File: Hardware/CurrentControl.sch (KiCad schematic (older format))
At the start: 24 parts, among them J4 Screw_Terminal_01x02, Q1 PSMN5R2-60YL, U3 DAC121C081CIMK, U4 TLV9102IPWR

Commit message: forgot to save
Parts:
- removed C16: 1n, Capacitor_SMD:C_0603_1608Metric_Pad1.05x0.95mm_HandSolder, symbol Device:C_Small
- removed U4: TLV9102IPWR, Package_SO:TSSOP-8_4.4x3mm_P0.65mm, symbol E-Load-rescue:TLV9102IPWR
- added R24: 5.6k, Resistor_SMD:R_0603_1608Metric_Pad1.05x0.95mm_HandSolder, symbol Device:R_Small
- added R26: 50k, Resistor_SMD:R_0603_1608Metric_Pad1.05x0.95mm_HandSolder, symbol Device:R_Small
- added TP1: TestPoint_Alt, TestPoint:TestPoint_Keystone_5000-5004_Miniature, symbol Connector:TestPoint_Alt
- added U4: MCP6H04, Package_SO:TSSOP-14_4.4x5mm_P0.65mm, symbol E-Load-rescue:MCP6H04
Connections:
- net labels added: Current_ADC, Vin_ADC
- net labels removed: ADC
- wire segments 60 -> 93
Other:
- moved on the sheet: C13, C15, C17, Q1, R10, R11, R12, R13, R20, R23, R25, R4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

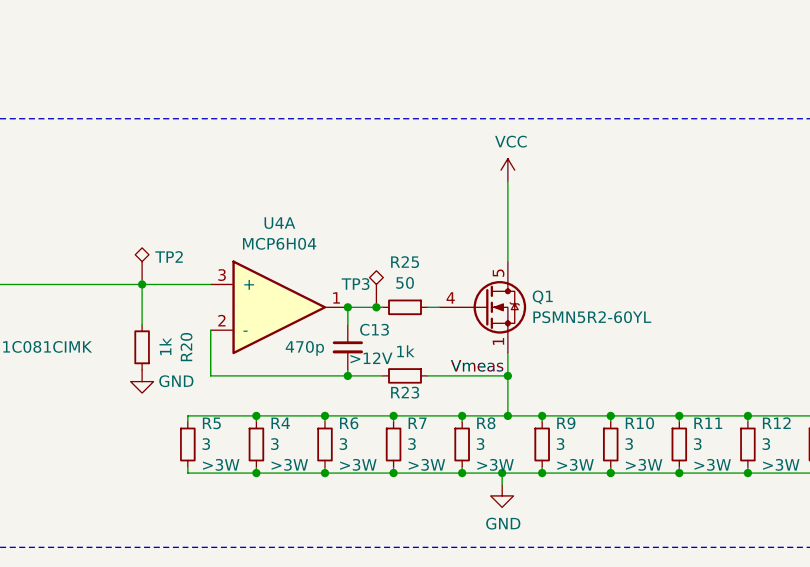
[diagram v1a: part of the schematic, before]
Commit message: Added LCSC part#, Thermal vias, etc
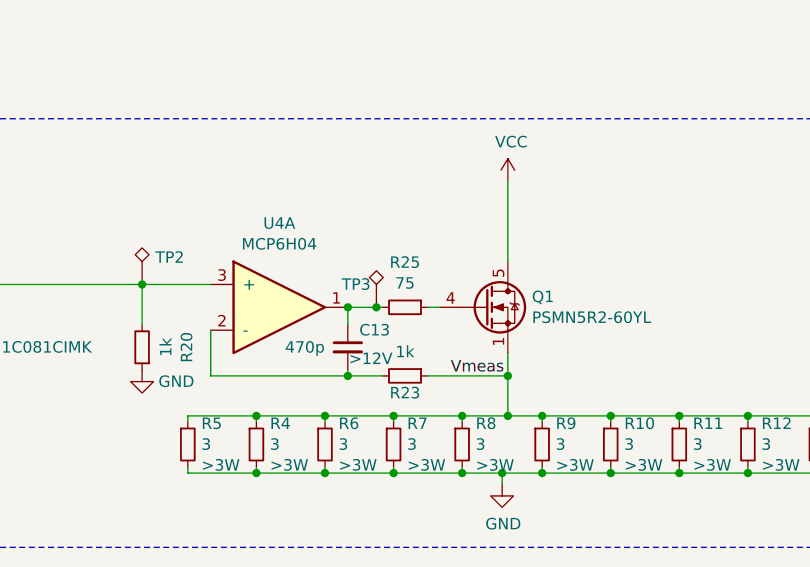
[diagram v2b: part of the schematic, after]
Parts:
- C13: LCSC (none) -> C376836
- C15, C17: LCSC (none) -> C100040
- J4: footprint Connector_TE-Connectivity:TE_826576-2_1x02_P3.96mm_Vertical -> Connector_Phoenix_MC:PhoenixContact_MCV_1,5_2-G-3.81_1x02_P3.81mm_Vertical; LCSC (none) -> C89123
- Q1: Digikey (none) -> 1727-2595-1-ND
- R10, R11, R12, R13, R4, R5, R6, R7, R8, R9: Digikey (none) -> PPC5W3.0CT-ND
- R20, R23: LCSC (none) -> C441891
- R24: LCSC (none) -> C507469
- R25: value 50 -> 75; LCSC (none) -> C441884
- R26: LCSC (none) -> C881419
- U3: Digikey (none) -> DAC121C081CIMK/NOPBCT-ND
- U4: Digikey (none) -> MCP6H04T-E/SLCT-ND
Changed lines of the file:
@@
 F 3 "~" H 3275 3850 50  0001 C CNN
 F 4 ">3W" H 3334 3759 50  0000 L CNN "Power "
+F 5 "PPC5W3.0CT-ND" H 3275 3850 50  0001 C CNN "Digikey"
 	1    3275 3850
 	1    0    0    -1
@@
 F 3 "~" H 3575 3850 50  0001 C CNN
 F 4 ">3W" H 3634 3759 50  0000 L CNN "Power "
+F 5 "PPC5W3.0CT-ND" H 3575 3850 50  0001 C CNN "Digikey"
 	1    3575 3850
 	1    0    0    -1
@@
 F 3 "~" H 3875 3850 50  0001 C CNN
 F 4 ">3W" H 3934 3759 50  0000 L CNN "Power "
+F 5 "PPC5W3.0CT-ND" H 3875 3850 50  0001 C CNN "Digikey"
 	1    3875 3850
 	1    0    0    -1
@@
 F 3 "~" H 4175 3850 50  0001 C CNN
 F 4 ">3W" H 4234 3759 50  0000 L CNN "Power "
+F 5 "PPC5W3.0CT-ND" H 4175 3850 50  0001 C CNN "Digikey"
 	1    4175 3850
 	1    0    0    -1
@@
 F 3 "~" H 4525 3850 50  0001 C CNN
 F 4 ">3W" H 4584 3759 50  0000 L CNN "Power "
+F 5 "PPC5W3.0CT-ND" H 4525 3850 50  0001 C CNN "Digikey"
 	1    4525 3850
 	1    0    0    -1
@@
 F 3 "~" H 4825 3850 50  0001 C CNN
 F 4 ">3W" H 4884 3759 50  0000 L CNN "Power "
+F 5 "PPC5W3.0CT-ND" H 4825 3850 50  0001 C CNN "Digikey"
 	1    4825 3850
 	1    0    0    -1
@@
 F 3 "~" H 5125 3850 50  0001 C CNN
 F 4 ">3W" H 5184 3759 50  0000 L CNN "Power "
+F 5 "PPC5W3.0CT-ND" H 5125 3850 50  0001 C CNN "Digikey"
 	1    5125 3850
 	1    0    0    -1
@@
 F 3 "~" H 5425 3850 50  0001 C CNN
 F 4 ">3W" H 5484 3759 50  0000 L CNN "Power "
+F 5 "PPC5W3.0CT-ND" H 5425 3850 50  0001 C CNN "Digikey"
 	1    5425 3850
 	1    0    0    -1
@@
 F 3 "~" H 5725 3850 50  0001 C CNN
 F 4 ">3W" H 5784 3759 50  0000 L CNN "Power "
+F 5 "PPC5W3.0CT-ND" H 5725 3850 50  0001 C CNN "Digikey"
 	1    5725 3850
 	1    0    0    -1
@@
 F 3 "~" H 2975 3850 50  0001 C CNN
 F 4 ">3W" H 3034 3759 50  0000 L CNN "Power "
+F 5 "PPC5W3.0CT-ND" H 2975 3850 50  0001 C CNN "Digikey"
 	1    2975 3850
 	1    0    0    -1
@@
 F 3 "~" H 10225 2950 50  0001 C CNN
 F 4 ">12V" H 10325 2850 50  0000 C CNN "Voltage"
+F 5 "" H 10225 2950 50  0001 C CNN "Digikey"
+F 6 "C100040" H 10225 2950 50  0001 C CNN "LCSC"
 	1    10225 2950
 	1    0    0    -1
@@
 P 3925 3250
 F 0 "R25" V 3729 3250 50  0000 C CNN
-F 1 "50" V 3820 3250 50  0000 C CNN
+F 1 "75" V 3820 3250 50  0000 C CNN
 F 2 "Resistor_SMD:R_0603_1608Metric_Pad1.05x0.95mm_HandSolder" H 3925 3250 50  0001 C CNN
 F 3 "~" H 3925 3250 50  0001 C CNN
+F 4 "" V 3925 3250 50  0001 C CNN "Digikey"
+F 5 "C441884" V 3925 3250 50  0001 C CNN "LCSC"
 	1    3925 3250
 	0    1    1    0
@@
 F 3 "~" H 10850 2950 50  0001 C CNN
 F 4 ">12V" H 10975 2850 50  0000 C CNN "Voltage"
+F 5 "" H 10850 2950 50  0001 C CNN "Digikey"
+F 6 "C100040" H 10850 2950 50  0001 C CNN "LCSC"
 	1    10850 2950
 	1    0    0    -1
@@
 F 2 "Package_TO_SOT_SMD:SOT-23-6" H 2375 2900 50  0001 C CNN
 F 3 "http://www.ti.com/lit/ds/symlink/dac121c081.pdf" H 1725 3150 50  0001 C CNN
+F 4 "DAC121C081CIMK/NOPBCT-ND" H 1725 3150 50  0001 C CNN "Digikey"
+F 5 "" H 1725 3150 50  0001 C CNN "LCSC"
 	1    1725 3150
 	1    0    0    -1
@@
 F 2 "Resistor_SMD:R_0603_1608Metric_Pad1.05x0.95mm_HandSolder" H 2775 3425 50  0001 C CNN
 F 3 "~" H 2775 3425 50  0001 C CNN
+F 4 "" V 2775 3425 50  0001 C CNN "Digikey"
+F 5 "C441891" V 2775 3425 50  0001 C CNN "LCSC"
 	1    2775 3425
 	-1   0    0    1
@@
 F 2 "Resistor_SMD:R_0603_1608Metric_Pad1.05x0.95mm_HandSolder" H 3925 3550 50  0001 C CNN
 F 3 "~" H 3925 3550 50  0001 C CNN
+F 4 "" V 3925 3550 50  0001 C CNN "Digikey"
+F 5 "C441891" V 3925 3550 50  0001 C CNN "LCSC"
 	1    3925 3550
 	0    1    1    0
@@
 F 3 "~" H 3675 3425 50  0001 C CNN
 F 4 ">12V" H 3775 3375 50  0000 C CNN "Voltage"
+F 5 "" H 3675 3425 50  0001 C CNN "Digikey"
+F 6 "C376836" H 3675 3425 50  0001 C CNN "LCSC"
 	1    3675 3425
 	1    0    0    -1
@@
 F 2 "Package_TO_SOT_SMD:LFPAK56" H 4425 3250 50  0001 C CNN
 F 3 "https://assets.nexperia.com/documents/data-sheet/PSMN5R2-60YL.pdf" H 4275 3250 50  0001 C CNN
+F 4 "1727-2595-1-ND" H 4275 3250 50  0001 C CNN "Digikey"
 	1    4275 3250
 	1    0    0    -1
@@
 F 0 "J4" H 6680 1217 50  0000 L CNN
 F 1 "Screw_Terminal_01x02" H 6680 1126 50  0000 L CNN
-F 2 "Connector_TE-Connectivity:TE_826576-2_1x02_P3.96mm_Vertical" H 6600 1225 50  0001 C CNN
+F 2 "Connector_Phoenix_MC:PhoenixContact_MCV_1,5_2-G-3.81_1x02_P3.81mm_Vertical" H 6600 1225 50  0001 C CNN
 F 3 "~" H 6600 1225 50  0001 C CNN
+F 4 "" H 6600 1225 50  0001 C CNN "Digikey"
+F 5 "C89123" H 6600 1225 50  0001 C CNN "LCSC"
 	1    6600 1225
 	1    0    0    -1
@@
 F 2 "Package_SO:TSSOP-14_4.4x5mm_P0.65mm" H 3375 3250 50  0001 C CNN
 F 3 "" H 3375 3250 50  0001 C CNN
+F 4 "MCP6H04T-E/SLCT-ND" H 3375 3250 50  0001 C CNN "Digikey"
+F 5 "" H 3375 3250 50  0001 C CNN "LCSC"
 	1    3375 3250
 	1    0    0    -1
@@
 F 2 "Resistor_SMD:R_0603_1608Metric_Pad1.05x0.95mm_HandSolder" H 7150 3500 50  0001 C CNN
 F 3 "~" H 7150 3500 50  0001 C CNN
+F 4 "" V 7150 3500 50  0001 C CNN "Digikey"
+F 5 "C507469" V 7150 3500 50  0001 C CNN "LCSC"
 	1    7150 3500
 	-1   0    0    1
@@
 F 2 "Resistor_SMD:R_0603_1608Metric_Pad1.05x0.95mm_HandSolder" H 7150 3850 50  0001 C CNN
 F 3 "~" H 7150 3850 50  0001 C CNN
+F 4 "" V 7150 3850 50  0001 C CNN "Digikey"
+F 5 "C881419" V 7150 3850 50  0001 C CNN "LCSC"
 	1    7150 3850
 	-1   0    0    1

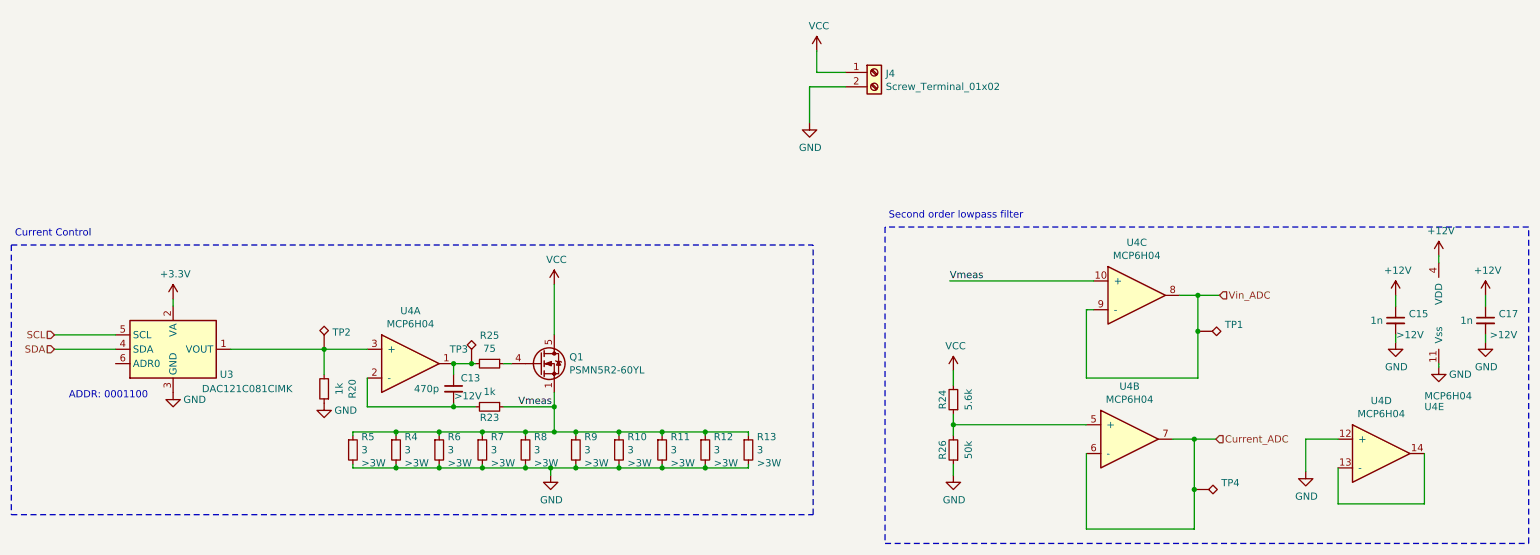
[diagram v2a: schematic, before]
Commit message: Added second mosfet and added FPaste layer on thermal vias
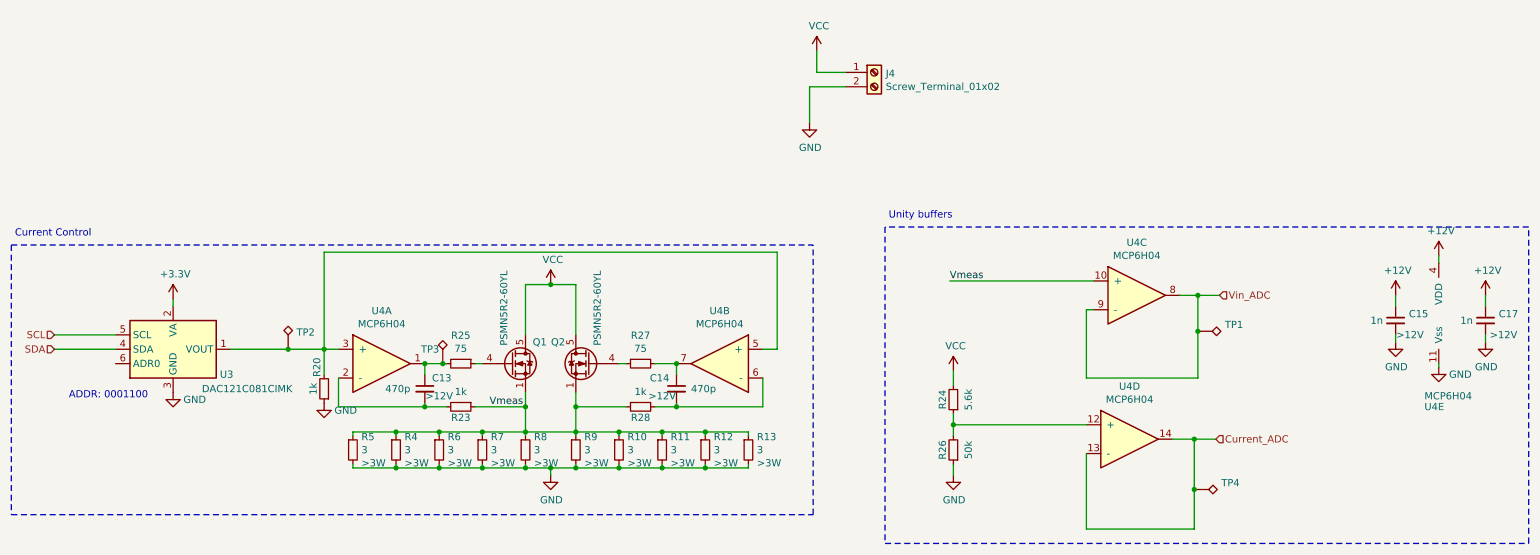
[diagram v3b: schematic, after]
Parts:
- removed unit 4 of U4
- added C14: 470p, Capacitor_SMD:C_0603_1608Metric_Pad1.05x0.95mm_HandSolder, symbol Device:C_Small
- added Q2: PSMN5R2-60YL, Package_TO_SOT_SMD:LFPAK56, symbol Transistor_FET:PSMN5R2-60YL
- added R27: 75, Resistor_SMD:R_0603_1608Metric_Pad1.05x0.95mm_HandSolder, symbol Device:R_Small
- added R28: 1k, Resistor_SMD:R_0603_1608Metric_Pad1.05x0.95mm_HandSolder, symbol Device:R_Small
- added unit 2 of U4
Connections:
- net Current_ADC: now also U4.13 (-), U4.14; no longer U4.6 (-), U4.7
- net VCC: now also Q2.5 (D)
- net Vmeas: now also Q2.1 (S), Q2.2 (S), Q2.3 (S), R28.1
- net at R20.2, TP2.1, U3.1 (VOUT)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: now also U4.5 (+)
- net at R24.1, R26.2: now also U4.12 (+); no longer U4.5 (+)
- new net: Q2.4 (G), R27.1
- new net: C14.1, R27.2, U4.7
- new net: C14.2, R28.2, U4.6 (-)
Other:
- note added: "Unity buffers"
- note removed: "Second order lowpass filter"
- moved on the sheet: C13, Q1, R23, R25, TP2, TP3, U4A

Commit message: Added PDF and other cleanup
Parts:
- added J5, J6: Conn_01x02_Male, Connector_PinHeader_2.54mm:PinHeader_1x02_P2.54mm_Vertical, symbol Connector:Conn_01x02_Male
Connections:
- net +12V: now also J5.1 (Pin_1), J6.1 (Pin_1)
- net GND: now also J5.2 (Pin_2), J6.2 (Pin_2)
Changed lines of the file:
@@
 Wire Wire Line
 	5925 3150 5825 3150
+$Comp
+L Connector:Conn_01x02_Male J5
+U 1 1 5FAF7BE1
+P 8250 1200
+F 0 "J5" H 8358 1381 50  0000 C CNN
+F 1 "Conn_01x02_Male" H 8358 1290 50  0000 C CNN
+F 2 "Connector_PinHeader_2.54mm:PinHeader_1x02_P2.54mm_Vertical" H 8250 1200 50  0001 C CNN
+F 3 "~" H 8250 1200 50  0001 C CNN
+	1    8250 1200
+	1    0    0    -1
+$EndComp
+$Comp
+L Connector:Conn_01x02_Male J6
+U 1 1 5FAF92D6
+P 8975 1200
+F 0 "J6" H 9083 1381 50  0000 C CNN
+F 1 "Conn_01x02_Male" H 9083 1290 50  0000 C CNN
+F 2 "Connector_PinHeader_2.54mm:PinHeader_1x02_P2.54mm_Vertical" H 8975 1200 50  0001 C CNN
+F 3 "~" H 8975 1200 50  0001 C CNN
+	1    8975 1200
+	1    0    0    -1
+$EndComp
+$Comp
+L power:+12V #PWR0138
+U 1 1 5FAFC078
+P 8525 1025
+F 0 "#PWR0138" H 8525 875 50  0001 C CNN
+F 1 "+12V" H 8540 1198 50  0000 C CNN
+F 2 "" H 8525 1025 50  0001 C CNN
+F 3 "" H 8525 1025 50  0001 C CNN
+	1    8525 1025
+	1    0    0    -1
+$EndComp
+$Comp
+L power:+12V #PWR0140
+U 1 1 5FAFC9A7
+P 9275 1025
+F 0 "#PWR0140" H 9275 875 50  0001 C CNN
+F 1 "+12V" H 9290 1198 50  0000 C CNN
+F 2 "" H 9275 1025 50  0001 C CNN
+F 3 "" H 9275 1025 50  0001 C CNN
+	1    9275 1025
+	1    0    0    -1
+$EndComp
+Wire Wire Line
+	8525 1025 8525 1200
+Wire Wire Line
+	8525 1200 8450 1200
+Wire Wire Line
+	9275 1025 9275 1200
+Wire Wire Line
+	9275 1200 9175 1200
+$Comp
+L power:GND #PWR0141
+U 1 1 5FB036CC
+P 8525 1450
+F 0 "#PWR0141" H 8525 1200 50  0001 C CNN
+F 1 "GND" H 8530 1277 50  0000 C CNN
+F 2 "" H 8525 1450 50  0001 C CNN
+F 3 "" H 8525 1450 50  0001 C CNN
+	1    8525 1450
+	1    0    0    -1
+$EndComp
+$Comp
+L power:GND #PWR0142
+U 1 1 5FB04054
+P 9275 1450
+F 0 "#PWR0142" H 9275 1200 50  0001 C CNN
+F 1 "GND" H 9280 1277 50  0000 C CNN
+F 2 "" H 9275 1450 50  0001 C CNN
+F 3 "" H 9275 1450 50  0001 C CNN
+	1    9275 1450
+	1    0    0    -1
+$EndComp
+Wire Wire Line
+	8450 1300 8525 1300
+Wire Wire Line
+	8525 1300 8525 1450
+Wire Wire Line
+	9175 1300 9275 1300
+Wire Wire Line
+	9275 1300 9275 1450
 $EndSCHEMATC
